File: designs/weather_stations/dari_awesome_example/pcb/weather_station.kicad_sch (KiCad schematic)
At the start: 15 parts, among them J1 ST7735, J2 NEOPIXEL, J3 DHT22, J4 UART, SW1 F TO C, U1 WEMOS C3 MINI

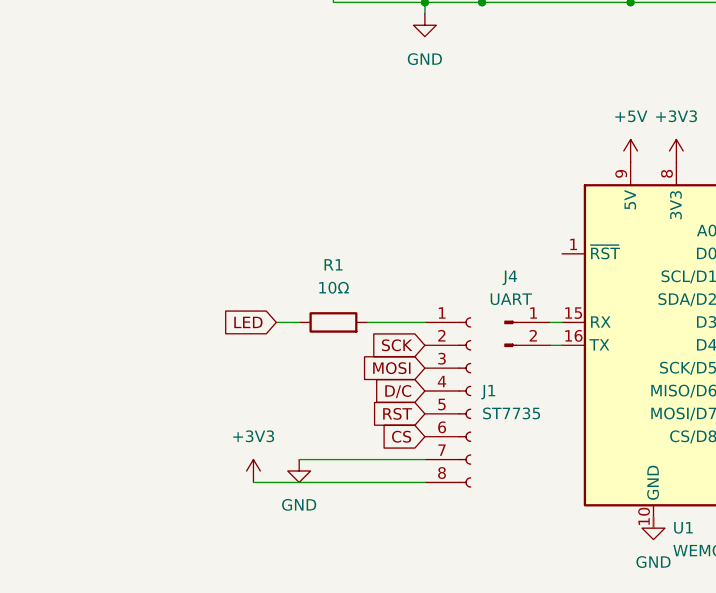
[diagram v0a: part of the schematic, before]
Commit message: updated weather station example
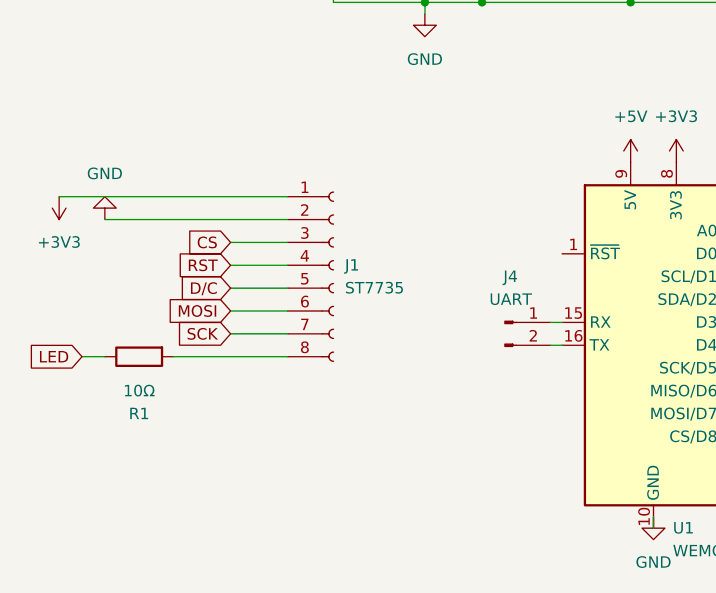
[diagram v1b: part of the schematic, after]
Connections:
- net +3V3: now also J1.1 (Pin_1); no longer J1.8 (Pin_8)
- net CS: now also J1.3 (Pin_3); no longer J1.6 (Pin_6)
- net D/C: now also J1.5 (Pin_5); no longer J1.4 (Pin_4)
- net GND: now also J1.2 (Pin_2); no longer J1.7 (Pin_7)
- net MOSI: now also J1.6 (Pin_6); no longer J1.3 (Pin_3)
- net RST: now also J1.4 (Pin_4); no longer J1.5 (Pin_5)
- net SCK: now also J1.7 (Pin_7); no longer J1.2 (Pin_2)
- net at R1.2: now also J1.8 (Pin_8); no longer J1.1 (Pin_1)
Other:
- moved on the sheet: J1, R1
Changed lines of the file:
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@@
+	(wire
+		(pts
+			(xy 50.8 68.58) (xy 57.15 68.58)
+		)
+		(stroke
+			(width 0)
+			(type default)
+		)
+	)
 	(wire
 		(pts
@@
 	(wire
 		(pts
-			(xy 58.42 90.17) (xy 72.39 90.17)
+			(xy 36.83 63.5) (xy 57.15 63.5)
 		)
 		(stroke
@@
 	(wire
 		(pts
+			(xy 57.15 66.04) (xy 50.8 66.04)
+		)
+		(stroke
+			(width 0)
+			(type default)
+		)
+	)
+	(wire
+		(pts
 			(xy 185.42 36.83) (xy 185.42 39.37)
 		)
@@
 	(wire
 		(pts
+			(xy 57.15 73.66) (xy 50.8 73.66)
+		)
+		(stroke
+			(width 0)
+			(type default)
+		)
+	)
+	(wire
+		(pts
 			(xy 127 60.96) (xy 127 64.77)
 		)
@@
 	(wire
 		(pts
+			(xy 57.15 76.2) (xy 50.8 76.2)
+		)
+		(stroke
+			(width 0)
+			(type default)
+		)
+	)
+	(wire
+		(pts
 			(xy 86.36 29.21) (xy 87.63 29.21)
 		)
@@
 	(wire
 		(pts
-			(xy 66.04 74.93) (xy 72.39 74.93)
+			(xy 44.45 78.74) (xy 57.15 78.74)
 		)
 		(stroke
@@
 	(wire
 		(pts
-			(xy 55.88 74.93) (xy 58.42 74.93)
+			(xy 34.29 78.74) (xy 36.83 78.74)
 		)
 		(stroke
@@
 	(wire
 		(pts
-			(xy 53.34 92.71) (xy 72.39 92.71)
+			(xy 31.75 60.96) (xy 57.15 60.96)
 		)
 		(stroke
@@
 		(pts
 			(xy 95.25 36.83) (xy 95.25 39.37)
+		)
+		(stroke
+			(width 0)
+			(type default)
+		)
+	)
+	(wire
+		(pts
+			(xy 57.15 71.12) (xy 50.8 71.12)
 		)
 		(stroke
@@
 	(global_label "D{slash}C"
 		(shape input)
-		(at 72.39 82.55 180)
+		(at 50.8 71.12 180)
 		(fields_autoplaced yes)
 		(effects
@@
 		)
 		(property "Intersheetrefs" "${INTERSHEET_REFS}"
-			(at 65.5343 82.55 0)
+			(at 43.9443 71.12 0)
 			(effects
 				(font
@@
 	(global_label "LED"
 		(shape input)
-		(at 55.88 74.93 180)
+		(at 34.29 78.74 180)
 		(fields_autoplaced yes)
 		(effects
@@
 		)
 		(property "Intersheetrefs" "${INTERSHEET_REFS}"
-			(at 49.4477 74.93 0)
+			(at 27.8577 78.74 0)
 			(effects
 				(font
@@
 	(global_label "CS"
 		(shape input)
-		(at 72.39 87.63 180)
+		(at 50.8 66.04 180)
 		(fields_autoplaced yes)
 		(effects
@@
 		)
 		(property "Intersheetrefs" "${INTERSHEET_REFS}"
-			(at 66.9253 87.63 0)
+			(at 45.3353 66.04 0)
 			(effects
 				(font
@@
 	(global_label "SCK"
 		(shape input)
-		(at 72.39 77.47 180)
+		(at 50.8 76.2 180)
 		(fields_autoplaced yes)
 		(effects
@@
 		)
 		(property "Intersheetrefs" "${INTERSHEET_REFS}"
-			(at 65.6553 77.47 0)
+			(at 44.0653 76.2 0)
 			(effects
 				(font
@@
 	(global_label "MOSI"
 		(shape input)
-		(at 72.39 80.01 180)
+		(at 50.8 73.66 180)
 		(fields_autoplaced yes)
 		(effects
@@
 		)
 		(property "Intersheetrefs" "${INTERSHEET_REFS}"
-			(at 64.8086 80.01 0)
+			(at 43.2186 73.66 0)
 			(effects
 				(font
@@
 	(global_label "RST"
 		(shape input)
-		(at 72.39 85.09 180)
+		(at 50.8 68.58 180)
 		(fields_autoplaced yes)
 		(effects
@@
 		)
 		(property "Intersheetrefs" "${INTERSHEET_REFS}"
-			(at 65.9577 85.09 0)
+			(at 44.3677 68.58 0)
 			(effects
 				(font
@@
 	(symbol
 		(lib_id "power:GND")
-		(at 58.42 90.17 0)
+		(at 36.83 63.5 0)
+		(mirror x)
 		(unit 1)
 		(exclude_from_sim no)
@@
 		(fields_autoplaced yes)
 		(property "Reference" "#PWR03"
-			(at 58.42 96.52 0)
+			(at 36.83 57.15 0)
 			(effects
 				(font
@@
 		)
 		(property "Value" "GND"
-			(at 58.42 95.25 0)
+			(at 36.83 58.42 0)
 			(effects
 				(font
@@
 		)
 		(property "Footprint" ""
-			(at 58.42 90.17 0)
+			(at 36.83 63.5 0)
 			(effects
 				(font
@@
 		)
 		(property "Datasheet" ""
-			(at 58.42 90.17 0)
+			(at 36.83 63.5 0)
 			(effects
 				(font
@@
 		)
 		(property "Description" "Power symbol creates a global label with name \"GND\" , ground"
-			(at 58.42 90.17 0)
+			(at 36.83 63.5 0)
 			(effects
 				(font
@@
 	(symbol
 		(lib_id "Connector:Conn_01x08_Socket")
-		(at 77.47 82.55 0)
+		(at 62.23 68.58 0)
 		(unit 1)
 		(exclude_from_sim no)
@@
 		(fields_autoplaced yes)
 		(property "Reference" "J1"
-			(at 78.74 82.5499 0)
+			(at 63.5 68.5799 0)
 			(effects
 				(font
@@
 		)
 		(property "Value" "ST7735"
-			(at 78.74 85.0899 0)
+			(at 63.5 71.1199 0)
 			(effects
 				(font
@@
 		)
 		(property "Footprint" "asylum-weather:TFT_ST7735_SD"
-			(at 77.47 82.55 0)
+			(at 62.23 68.58 0)
 			(effects
 				(font
@@
 		)
 		(property "Datasheet" "~"
-			(at 77.47 82.55 0)
+			(at 62.23 68.58 0)
 			(effects
 				(font
@@
 		)
 		(property "Description" "Generic connector, single row, 01x08, script generated"
-			(at 77.47 82.55 0)
+			(at 62.23 68.58 0)
 			(effects
 				(font
@@
 	(symbol
 		(lib_id "power:+3V3")
-		(at 53.34 92.71 0)
+		(at 31.75 60.96 0)
+		(mirror x)
 		(unit 1)
 		(exclude_from_sim no)
@@
 		(fields_autoplaced yes)
 		(property "Reference" "#PWR05"
-			(at 53.34 96.52 0)
+			(at 31.75 57.15 0)
 			(effects
 				(font
@@
 		)
 		(property "Value" "+3V3"
-			(at 53.34 87.63 0)
+			(at 31.75 66.04 0)
 			(effects
 				(font
@@
 		)
 		(property "Footprint" ""
-			(at 53.34 92.71 0)
+			(at 31.75 60.96 0)
 			(effects
 				(font
@@
 		)
 		(property "Datasheet" ""
-			(at 53.34 92.71 0)
+			(at 31.75 60.96 0)
 			(effects
 				(font
@@
 		)
 		(property "Description" "Power symbol creates a global label with name \"+3V3\""
-			(at 53.34 92.71 0)
+			(at 31.75 60.96 0)
 			(effects
 				(font
@@
 	(symbol
 		(lib_id "Device:R")
-		(at 62.23 74.93 90)
+		(at 40.64 78.74 90)
+		(mirror x)
 		(unit 1)
 		(exclude_from_sim no)
@@
 		(fields_autoplaced yes)
 		(property "Reference" "R1"
-			(at 62.23 68.58 90)
+			(at 40.64 85.09 90)
 			(effects
 				(font
@@
 		)
 		(property "Value" "10Ω"
-			(at 62.23 71.12 90)
+			(at 40.64 82.55 90)
 			(effects
 				(font
@@
 		)
 		(property "Footprint" "Resistor_THT:R_Axial_DIN0207_L6.3mm_D2.5mm_P7.62mm_Horizontal"
-			(at 62.23 76.708 90)
+			(at 40.64 76.962 90)
 			(effects
 				(font
@@
 		)
 		(property "Datasheet" "~"
-			(at 62.23 74.93 0)
+			(at 40.64 78.74 0)
 			(effects
 				(font
@@
 		)
 		(property "Description" "Resistor"
-			(at 62.23 74.93 0)
-			(effects
-				(font
+			(at 40.64 78.74 0)
+			(effects
+				(font
